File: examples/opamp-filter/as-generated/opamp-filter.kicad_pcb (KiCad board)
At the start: 2 copper layers, 58 x 42 mm, 22 parts, among them J1 IN, J2 5V, J3 OUT, U1 MCP6001R, U2 MCP6001R

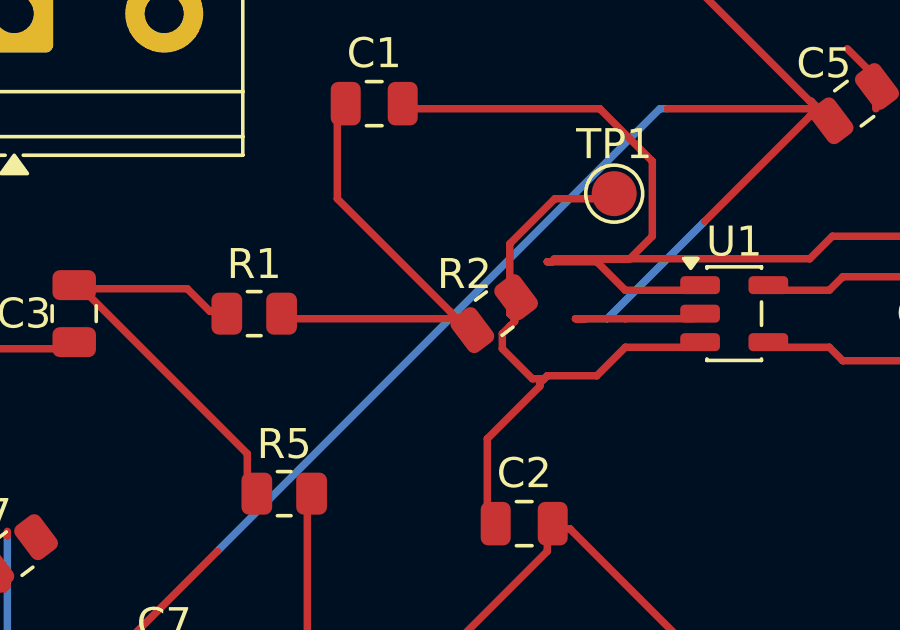
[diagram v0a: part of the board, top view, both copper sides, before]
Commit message: Take out the copper a run lays down and walks back along
Joining two routes at a shared end left the polyline going out past the
join and straight back to it. That is the zero-degree corner
route.acute_angle was reporting on the opamp and the motor board, and on
the plot it reads as a spur with no explanation, because it is one - the
overshoot carries no current.

Only an exact reversal that stops short of where it set out from, and
never a corner another track ends on: that is a join, however it looks.
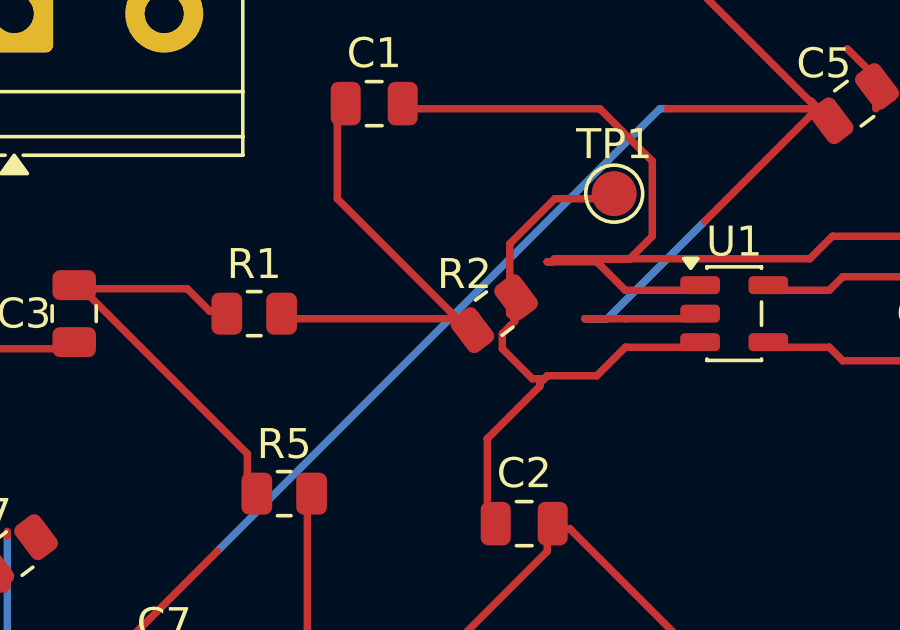
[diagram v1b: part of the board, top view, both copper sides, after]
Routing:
- net +5V: track 97.5 -> 96.9 mm
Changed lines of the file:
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@@
 	(segment (start 128.65 75.1) (end 127.0 75.1) (width 0.25) (layer "F.Cu") (net 7))
 	(segment (start 131.8625 77.0) (end 129.6 77.0) (width 0.25) (layer "F.Cu") (net 2))
-	(segment (start 129.6 77.0) (end 127.938 77.0) (width 0.25) (layer "F.Cu") (net 2))
-	(segment (start 127.938 77.0) (end 128.25 77.0) (width 0.25) (layer "F.Cu") (net 2))
+	(segment (start 129.6 77.0) (end 128.25 77.0) (width 0.25) (layer "F.Cu") (net 2))
 	(segment (start 131.8625 77.95) (end 129.6 77.95) (width 0.25) (layer "F.Cu") (net 3))
 	(segment (start 129.6 77.95) (end 128.65 78.9) (width 0.25) (layer "F.Cu") (net 3))
@@
 	(segment (start 117.0 82.75) (end 117.0 82.9125) (width 0.25) (layer "F.Cu") (net 5))
 	(segment (start 117.0 82.9125) (end 117.0875 83.0) (width 0.25) (layer "F.Cu") (net 5))
-	(segment (start 117.9125 77.0) (end 124.0875 77.0) (width 0.25) (layer "F.Cu") (net 10))
-	(segment (start 124.0875 77.0) (end 124.0 77.0) (width 0.25) (layer "F.Cu") (net 10))
-	(segment (start 124.0 77.0) (end 123.75 76.75) (width 0.25) (layer "F.Cu") (net 10))
+	(segment (start 117.9125 77.0) (end 123.823 77.0) (width 0.25) (layer "F.Cu") (net 10))
+	(segment (start 123.823 77.0) (end 123.823 76.927) (width 0.25) (layer "F.Cu") (net 10))
+	(segment (start 123.823 76.927) (end 123.875 76.875) (width 0.25) (layer "F.Cu") (net 10))
+	(segment (start 123.875 76.875) (end 123.75 76.75) (width 0.25) (layer "F.Cu") (net 10))
 	(segment (start 123.75 76.75) (end 120.0 73.0) (width 0.25) (layer "F.Cu") (net 10))
 	(segment (start 120.0 73.0) (end 120.0 70.25) (width 0.25) (layer "F.Cu") (net 10))

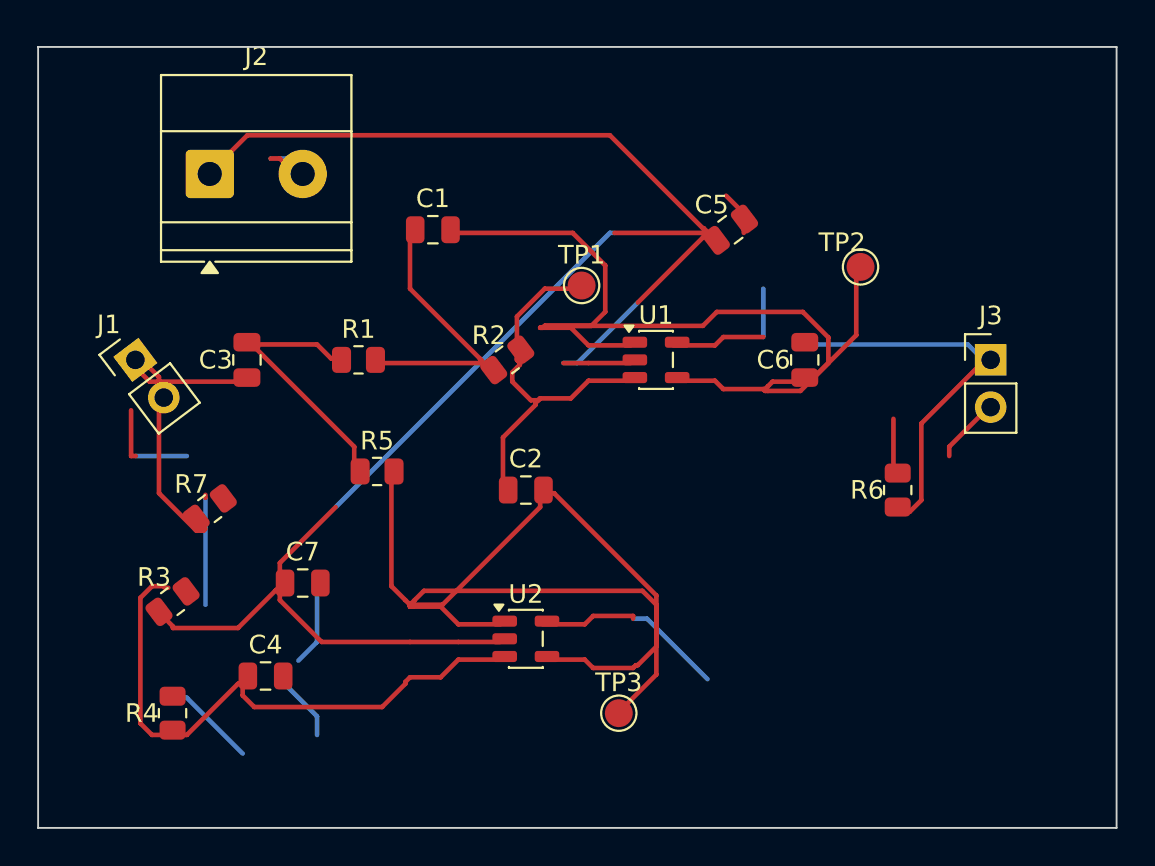
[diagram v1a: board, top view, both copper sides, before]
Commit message: Give the motor board a floorplan its signals can be routed on
The right hand third was a horseshoe: four logic signals leaving the
package on the east side went up over the top of the board, round the
outside and back into the header from behind - 190 mm of copper for a
40 mm net, and four short back-layer runs each cutting the plane under
the track that fed it. The router was not being stupid. The corridor
between the package and the header was walled off by the VM chain
running from the bulk cap down to the charge pump, and going round was
the only way through.

So the floorplan says what it means now. The header sits where the fan
lands, pin for pin and in the same order, so the four inputs run
straight across. The three small caps sit in the middle band with the
supply pins that own them, and the logic passes above and below them.
The bulk cap and the input terminal are at the top edge, out of the way.

That leaves VM needing to reach the middle of a row the logic leaves
from either side of. On two layers something has to cross, and the
choice is which: four signals going round the world, or one stated link
on the back for the rail. The rail is the right answer - it is low
impedance, the plane it crosses is its own return, and the signals cross
the cut it leaves at right angles, a track width each rather than a
detour. It is in the file as a link, not as something a search stumbled
into.

Ground leaves the fan and takes one more step before dropping into the
plane, because on top of a 0.65 mm escape the pour is whatever fits
between two lanes - a strip too thin to reach anything. Stitching vias
now ask for the same thing: a clearance plus a sliver's worth of copper
to hold on to, rather than the clearance alone.

route.return_path 4 -> 0, route.detour 1 -> 0, route.acute_angle 1 -> 0,
layout.pour_fragmented 1 -> 0, track.thin_power and route.width_step to
zero. The zone-island DRC errors are older than this change and still
there; they are the fill's own problem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
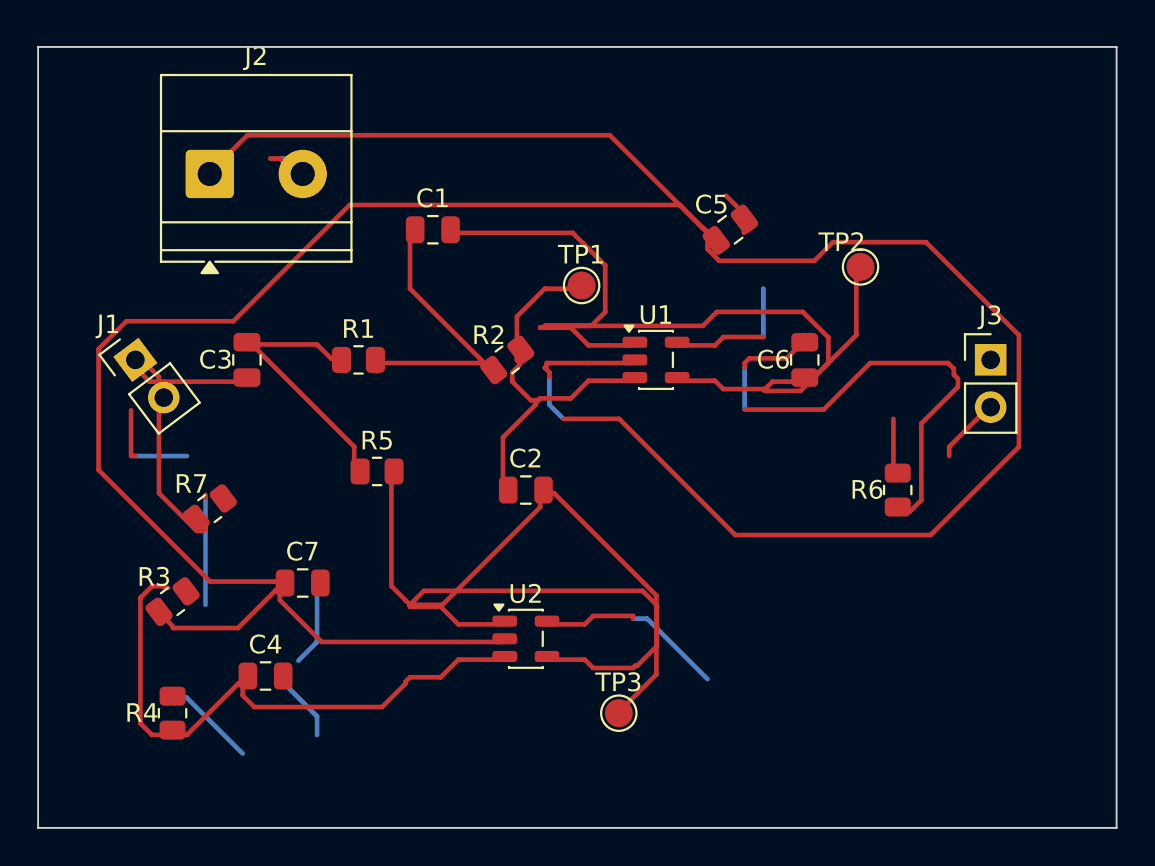
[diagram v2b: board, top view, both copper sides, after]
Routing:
- net +5V: track 96.9 -> 169.8 mm
- net /OUT_AC: track 21.2 -> 28.1 mm
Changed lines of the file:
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@@
 	(segment (start 128.65 75.1) (end 127.0 75.1) (width 0.25) (layer "F.Cu") (net 7))
 	(segment (start 131.8625 77.0) (end 129.6 77.0) (width 0.25) (layer "F.Cu") (net 2))
-	(segment (start 129.6 77.0) (end 128.25 77.0) (width 0.25) (layer "F.Cu") (net 2))
+	(segment (start 129.6 77.0) (end 127.354 77.0) (width 0.25) (layer "F.Cu") (net 2))
+	(segment (start 127.354 77.0) (end 127.354 77.146) (width 0.25) (layer "F.Cu") (net 2))
+	(segment (start 127.354 77.146) (end 127.25 77.25) (width 0.25) (layer "F.Cu") (net 2))
+	(segment (start 127.25 77.25) (end 127.5 77.5) (width 0.25) (layer "F.Cu") (net 2))
+	(segment (start 127.5 77.5) (end 127.5 77.75) (width 0.25) (layer "F.Cu") (net 2))
 	(segment (start 131.8625 77.95) (end 129.6 77.95) (width 0.25) (layer "F.Cu") (net 3))
 	(segment (start 129.6 77.95) (end 128.65 78.9) (width 0.25) (layer "F.Cu") (net 3))
@@
 	(segment (start 130.5 71.75) (end 128.75 70.0) (width 0.25) (layer "F.Cu") (net 7))
 	(segment (start 128.75 70.0) (end 121.95 70.0) (width 0.25) (layer "F.Cu") (net 7))
-	(segment (start 141.0 76.05) (end 141.2 76.05) (width 0.25) (layer "F.Cu") (net 8))
-	(segment (start 141.2 76.05) (end 141.25 76.0) (width 0.25) (layer "F.Cu") (net 8))
-	(segment (start 141.25 76.0) (end 150.0 76.0) (width 0.25) (layer "B.Cu") (net 8))
-	(segment (start 150.0 76.0) (end 151.0 77.0) (width 0.25) (layer "B.Cu") (net 8))
-	(segment (start 151.0 77.0) (end 150.75 77.0) (width 0.25) (layer "F.Cu") (net 8))
-	(segment (start 150.75 77.0) (end 147.5 80.25) (width 0.25) (layer "F.Cu") (net 8))
+	(segment (start 141.0 76.05) (end 140.95 76.05) (width 0.25) (layer "F.Cu") (net 8))
+	(segment (start 140.95 76.05) (end 140.75 76.25) (width 0.25) (layer "F.Cu") (net 8))
+	(segment (start 140.75 76.25) (end 140.25 76.75) (width 0.25) (layer "F.Cu") (net 8))
+	(segment (start 140.25 76.75) (end 138.25 76.75) (width 0.25) (layer "F.Cu") (net 8))
+	(segment (start 138.25 76.75) (end 138.0 77.0) (width 0.25) (layer "F.Cu") (net 8))
+	(segment (start 138.0 77.0) (end 138.0 77.25) (width 0.25) (layer "F.Cu") (net 8))
+	(segment (start 138.0 77.25) (end 138.0 79.5) (width 0.25) (layer "B.Cu") (net 8))
+	(segment (start 138.0 79.5) (end 142.25 79.5) (width 0.25) (layer "F.Cu") (net 8))
+	(segment (start 142.25 79.5) (end 144.75 77.0) (width 0.25) (layer "F.Cu") (net 8))
+	(segment (start 144.75 77.0) (end 148.939 77.0) (width 0.25) (layer "F.Cu") (net 8))
+	(segment (start 148.939 77.0) (end 149.25 77.311) (width 0.25) (layer "F.Cu") (net 8))
+	(segment (start 149.25 77.311) (end 149.25 77.622) (width 0.25) (layer "F.Cu") (net 8))
+	(segment (start 149.25 77.622) (end 149.469 77.841) (width 0.25) (layer "F.Cu") (net 8))
+	(segment (start 149.469 77.841) (end 149.469 78.28) (width 0.25) (layer "F.Cu") (net 8))
+	(segment (start 149.469 78.28) (end 147.5 80.25) (width 0.25) (layer "F.Cu") (net 8))
 	(segment (start 147.5 80.25) (end 147.5 84.375) (width 0.25) (layer "F.Cu") (net 8))
 	(segment (start 147.5 84.375) (end 146.875 85.0) (width 0.25) (layer "F.Cu") (net 8))
@@
 	(segment (start 135.75 69.75) (end 135.8 69.75) (width 0.25) (layer "F.Cu") (net 2))
 	(segment (start 135.8 69.75) (end 136.05 70.0) (width 0.25) (layer "F.Cu") (net 2))
+	(segment (start 136.05 70.0) (end 136.05 70.2) (width 0.25) (layer "F.Cu") (net 2))
+	(segment (start 136.05 70.2) (end 136.0 70.25) (width 0.25) (layer "F.Cu") (net 2))
+	(segment (start 136.0 70.25) (end 136.0 70.875) (width 0.25) (layer "F.Cu") (net 2))
+	(segment (start 136.0 70.875) (end 136.625 71.5) (width 0.25) (layer "F.Cu") (net 2))
+	(segment (start 136.625 71.5) (end 141.75 71.5) (width 0.25) (layer "F.Cu") (net 2))
+	(segment (start 141.75 71.5) (end 142.75 70.5) (width 0.25) (layer "F.Cu") (net 2))
+	(segment (start 142.75 70.5) (end 147.75 70.5) (width 0.25) (layer "F.Cu") (net 2))
+	(segment (start 147.75 70.5) (end 152.75 75.5) (width 0.25) (layer "F.Cu") (net 2))
+	(segment (start 152.75 75.5) (end 152.75 81.5) (width 0.25) (layer "F.Cu") (net 2))
+	(segment (start 152.75 81.5) (end 148.0 86.25) (width 0.25) (layer "F.Cu") (net 2))
+	(segment (start 148.0 86.25) (end 137.5 86.25) (width 0.25) (layer "F.Cu") (net 2))
+	(segment (start 137.5 86.25) (end 131.25 80.0) (width 0.25) (layer "F.Cu") (net 2))
+	(segment (start 131.25 80.0) (end 128.25 80.0) (width 0.25) (layer "F.Cu") (net 2))
+	(segment (start 128.25 80.0) (end 127.5 79.25) (width 0.25) (layer "B.Cu") (net 2))
+	(segment (start 127.5 79.25) (end 127.5 77.75) (width 0.25) (layer "B.Cu") (net 2))
 	(segment (start 136.05 70.0) (end 136.0 70.0) (width 0.25) (layer "F.Cu") (net 2))
-	(segment (start 136.0 70.0) (end 135.75 70.25) (width 0.25) (layer "F.Cu") (net 2))
-	(segment (start 135.75 70.25) (end 132.25 73.75) (width 0.25) (layer "F.Cu") (net 2))
-	(segment (start 132.25 73.75) (end 129.0 77.0) (width 0.25) (layer "B.Cu") (net 2))
-	(segment (start 129.0 77.0) (end 128.25 77.0) (width 0.25) (layer "B.Cu") (net 2))
-	(segment (start 136.05 70.0) (end 131.0 70.0) (width 0.25) (layer "F.Cu") (net 2))
-	(segment (start 131.0 70.0) (end 130.75 70.0) (width 0.25) (layer "B.Cu") (net 2))
-	(segment (start 130.75 70.0) (end 116.0 84.75) (width 0.25) (layer "B.Cu") (net 2))
-	(segment (start 116.0 84.75) (end 113.0 87.75) (width 0.25) (layer "F.Cu") (net 2))
-	(segment (start 113.0 87.75) (end 113.0 88.75) (width 0.25) (layer "F.Cu") (net 2))
-	(segment (start 113.0 88.75) (end 113.0 88.95) (width 0.25) (layer "F.Cu") (net 2))
-	(segment (start 113.0 88.95) (end 113.05 89.0) (width 0.25) (layer "F.Cu") (net 2))
+	(segment (start 136.0 70.0) (end 135.75 69.75) (width 0.25) (layer "F.Cu") (net 2))
+	(segment (start 135.75 69.75) (end 134.5 68.5) (width 0.25) (layer "F.Cu") (net 2))
+	(segment (start 134.5 68.5) (end 116.75 68.5) (width 0.25) (layer "F.Cu") (net 2))
+	(segment (start 116.75 68.5) (end 110.5 74.75) (width 0.25) (layer "F.Cu") (net 2))
+	(segment (start 110.5 74.75) (end 104.75 74.75) (width 0.25) (layer "F.Cu") (net 2))
+	(segment (start 104.75 74.75) (end 103.25 76.25) (width 0.25) (layer "F.Cu") (net 2))
+	(segment (start 103.25 76.25) (end 103.25 82.75) (width 0.25) (layer "F.Cu") (net 2))
+	(segment (start 103.25 82.75) (end 109.25 88.75) (width 0.25) (layer "F.Cu") (net 2))
+	(segment (start 109.25 88.75) (end 112.75 88.75) (width 0.25) (layer "F.Cu") (net 2))
+	(segment (start 112.75 88.75) (end 112.8 88.75) (width 0.25) (layer "F.Cu") (net 2))
+	(segment (start 112.8 88.75) (end 113.05 89.0) (width 0.25) (layer "F.Cu") (net 2))
 	(segment (start 113.05 89.0) (end 113.0 89.0) (width 0.25) (layer "F.Cu") (net 2))
 	(segment (start 113.0 89.0) (end 112.75 89.25) (width 0.25) (layer "F.Cu") (net 2))
